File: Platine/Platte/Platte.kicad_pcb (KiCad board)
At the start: 2 copper layers, 31.1 x 31.1 mm, 9 parts, among them J1 Conn_01x07_MountingPin

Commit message: Changes to plate PCB
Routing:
- added copper zone on B.Cu, net /analog_inp_high3
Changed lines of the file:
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@@
 		)
-	)
-	(gr_line
-		(start 85.75 65.75)
-		(end 111 65.75)
-		(stroke
-			(width 0.2)
-			(type default)
-		)
-		(layer "B.Cu")
-		(net 9)
 	)
 	(gr_arc
@@
 			(type default)
 		)
-		(layer "B.Paste")
+		(layer "B.Cu")
+		(net 12)
+	)
+	(gr_line
+		(start 85.75 65.75)
+		(end 111 65.75)
+		(stroke
+			(width 0.2)
+			(type default)
+		)
+		(layer "B.Cu")
+		(net 9)
 	)
 	(gr_arc
 		(start 85.720434 65.708995)
-		(mid 98.354418 56.213174)
+		(mid 98.354418 56.213173)
 		(end 111 65.693544)
 		(stroke
@@
 			(type default)
 		)
-		(layer "B.Paste")
+		(layer "B.Cu")
+		(net 9)
 	)
 	(gr_line
@@
 			(type default)
 		)
-		(layer "B.Paste")
+		(layer "B.Cu")
+		(net 10)
 	)
 	(gr_line
@@
 			(type default)
 		)
-		(layer "B.Paste")
+		(layer "B.Cu")
+		(net 12)
 	)
 	(gr_line
@@
 			(type default)
 		)
-		(layer "B.Paste")
+		(layer "B.Cu")
+		(net 10)
 	)
 	(gr_line
@@
 			(type default)
 		)
-		(layer "B.Paste")
+		(layer "B.Cu")
+		(net 10)
 	)
 	(gr_line
-		(start 85.75 67.5)
-		(end 111 67.5)
+		(start 91.5 67.5)
+		(end 97.25 67.5)
 		(stroke
 			(width 0.2)
 			(type default)
 		)
-		(layer "B.Paste")
+		(layer "B.Cu")
+		(net 10)
 	)
 	(gr_circle
@@
 			(pts
 				(xy 94.75 60.25) (xy 94.75 81.75) (xy 103.75 81.75) (xy 111 74.5) (xy 111 62.75) (xy 108.5 60.25)
-				(xy 94.75 60.25)
 			)
 		)
@@
 		(layer "B.Cu")
 		(hatch edge 0.5)
+		(priority 4)
 		(connect_pads
 			(clearance 0.5)
@@
 		(polygon
 			(pts
-				(xy 111 65.75) (xy 86 65.75) (xy 86 62.75) (xy 93.25 56) (xy 103.5 56) (xy 111 62.75)
+				(xy 85.75 65.75) (xy 111 65.75) (xy 110 63.25) (xy 109 61.5) (xy 107.25 59.75) (xy 105.5 58.25)
+				(xy 103 57) (xy 101.5 56.5) (xy 98.25 56.25) (xy 95.75 56.5) (xy 93.75 57) (xy 92.25 57.75) (xy 90.25 59)
+				(xy 88.5 60.75) (xy 87.5 62) (xy 86.75 63.25) (xy 86.25 64.25)
+			)
+		)
+	)
+	(zone
+		(net 12)
+		(net_name "/analog_inp_high3")
+		(layer "B.Cu")
+		(hatch edge 0.5)
+		(priority 3)
+		(connect_pads
+			(clearance 0.5)
+		)
+		(min_thickness 0.25)
+		(filled_areas_thickness no)
+		(fill yes
+			(thermal_gap 0.5)
+			(thermal_bridge_width 0.5)
+		)
+		(polygon
+			(pts
+				(xy 111 74.25) (xy 86 74.25) (xy 86 74.75) (xy 86.25 75) (xy 86.25 75.25) (xy 86.5 75.5) (xy 86.5 75.75)
+				(xy 86.75 76) (xy 86.75 76.25) (xy 87 76.5) (xy 87 76.75) (xy 87.25 77) (xy 87.4 77) (xy 87.4 77.2)
+				(xy 87.8 77.6) (xy 87.8 77.8) (xy 88 77.8) (xy 88 78.2) (xy 88.2 78.2) (xy 88.6 78.6) (xy 88.6 78.8)
+				(xy 88.8 79) (xy 89 79) (xy 89 79.2) (xy 89.2 79.2) (xy 89.2 79.4) (xy 89.4 79.4) (xy 90 80) (xy 90.4 80.2)
+				(xy 90.8 80.6) (xy 92.4 81.4) (xy 93 81.8) (xy 94.8 82.4) (xy 96.6 82.8) (xy 99.2 83) (xy 101.6 82.6)
+				(xy 103.8 81.8) (xy 105.8 80.8) (xy 107.2 79.8) (xy 108.8 78) (xy 109.6 77) (xy 110.2 76.2) (xy 110.8 74.8)
+				(xy 111 74.2)
 			)
 		)
@@
 		(polygon
 			(pts
-				(xy 111 64.75) (xy 86 64.75) (xy 86 64.25) (xy 86.5 63.75) (xy 86.5 62.75) (xy 87.75 61.5) (xy 87.75 61)
-				(xy 89.75 59) (xy 90.25 59) (xy 93.25 56) (xy 103.5 56) (xy 110.75 63.25) (xy 111 63.25)
+				(xy 111 74.25) (xy 110.25 76) (xy 108.25 78.75) (xy 106.25 80.5) (xy 104.5 81.5) (xy 103.5 82) (xy 100.5 82.75)
+				(xy 99 83) (xy 95 82.5) (xy 92.75 81.75) (xy 89.75 79.75) (xy 87.75 77.75) (xy 87 76.75) (xy 86 74.75)
+				(xy 85.8 74.2)
 			)
 		)
+	)
+	(zone
+		(net 0)
+		(net_name "")
+		(layer "B.Mask")
+		(hatch edge 0.5)
+		(connect_pads
+			(clearance 0.5)
+		)
+		(min_thickness 0.25)
+		(filled_areas_thickness no)
+		(fill yes
+			(thermal_gap 0.5)
+			(thermal_bridge_width 0.5)
+		)
+		(polygon
+			(pts
+				(xy 111 65.75) (xy 85.75 65.75) (xy 86.25 64.25) (xy 86.75 63.25) (xy 88.25 61) (xy 90 59.25) (xy 92.25 57.75)
+				(xy 93.25 57.25) (xy 94.75 56.75) (xy 96 56.5) (xy 98 56.25) (xy 99.75 56.25) (xy 101.75 56.75)
+				(xy 103.5 57.25) (xy 105 58) (xy 107 59.5) (xy 109 61.5) (xy 110.25 63.75) (xy 110.75 65)
+			)
+		)

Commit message: Plate PCB almost done
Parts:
- moved C1 0.96 mm to (88.8, 73.2), turned to -90 degrees
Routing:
- net /analog_inp_high2: track 2.09 -> 8.81 mm, vias 0 -> 5
- net /analog_inp_high3: track 1.79 -> 6.03 mm, vias 0 -> 3
- net GNDA: track 15.3 -> 17.6 mm
- net /analog_inp_high1: track 5.12 -> 7.17 mm, vias 2 -> 4
- net +3.3V: track 45.5 -> 44.5 mm
- added copper zone on B.Cu, net /analog_inp_high2
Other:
- board text added: "I 3.3V O Clk O Da1 O Da2 O Da3 O GNDD I GNDA"
- board text added: "Platte v1.0 EST RUB"

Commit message: small changes
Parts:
- J1: value Conn_01x07_MountingPin -> Conn_01x08_MountingPin; footprint Connector_JST:JST_GH_BM07B-GHS-TBT_1x07-1MP_P1.25mm_Vertical -> Connector_JST:JST_GH_BM08B-GHS-TBT_1x08-1MP_P1.25mm_Vertical
- R1, R2, R3: footprint Resistor_SMD:R_01005_0402Metric_Pad0.57x0.30mm_HandSolder -> Resistor_SMD:R_0201_0603Metric_Pad0.64x0.40mm_HandSolder
- moved J1 0.61 mm to (105.2, 68.0)
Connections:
- J1 pad 1: +3.3V -> VCC
- J1 pad 2: /out_clock -> +3.3V
- J1 pad 3: /amp_data1 -> /out_clock
- J1 pad 4: /amp_data2 -> /amp_data1
- J1 pad 5: /amp_data3 -> /amp_data2
- J1 pad 6: GNDD -> /amp_data3
- J1 pad 7: GNDA -> GNDD
- R1 pad 1: /analog_inp_low1 -> VCC
- R2 pad 1: /analog_inp_low2 -> VCC
- R3 pad 1: /analog_inp_low3 -> VCC
- U1 pad 3: /analog_inp_low1 -> VCC
- U2 pad 3: /analog_inp_low2 -> VCC
- U3 pad 3: /analog_inp_low3 -> VCC
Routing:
- net VCC: track 0.00 -> 6.01 mm
- net /analog_inp_low1: track 2.04 -> 0.00 mm
- net /analog_inp_low2: track 2.01 -> 0.00 mm
- net /analog_inp_low3: track 1.96 -> 0.00 mm
- net /analog_inp_high1: track 7.17 -> 6.17 mm
- net /analog_inp_high3: track 6.03 -> 5.08 mm
- net /analog_inp_high2: track 8.81 -> 8.09 mm
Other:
- board text added: "I VPlate I 3.3V O Clk O Da1 O Da2 O Da3 O GNDD I GNDA"
- board text removed: "I 3.3V O Clk O Da1 O Da2 O Da3 O GNDD I GNDA"

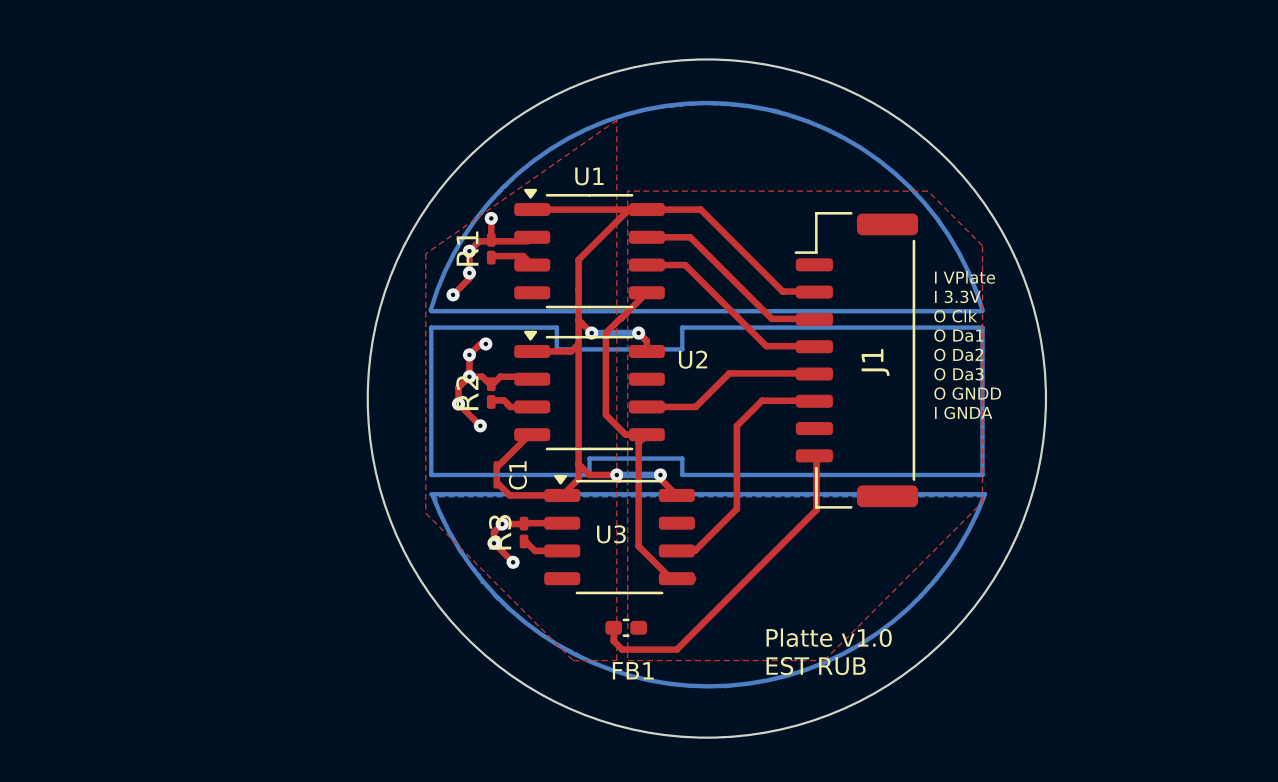
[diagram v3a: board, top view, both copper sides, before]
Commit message: Removing CST simulations because of weight, theyre now in the folder outside the repo
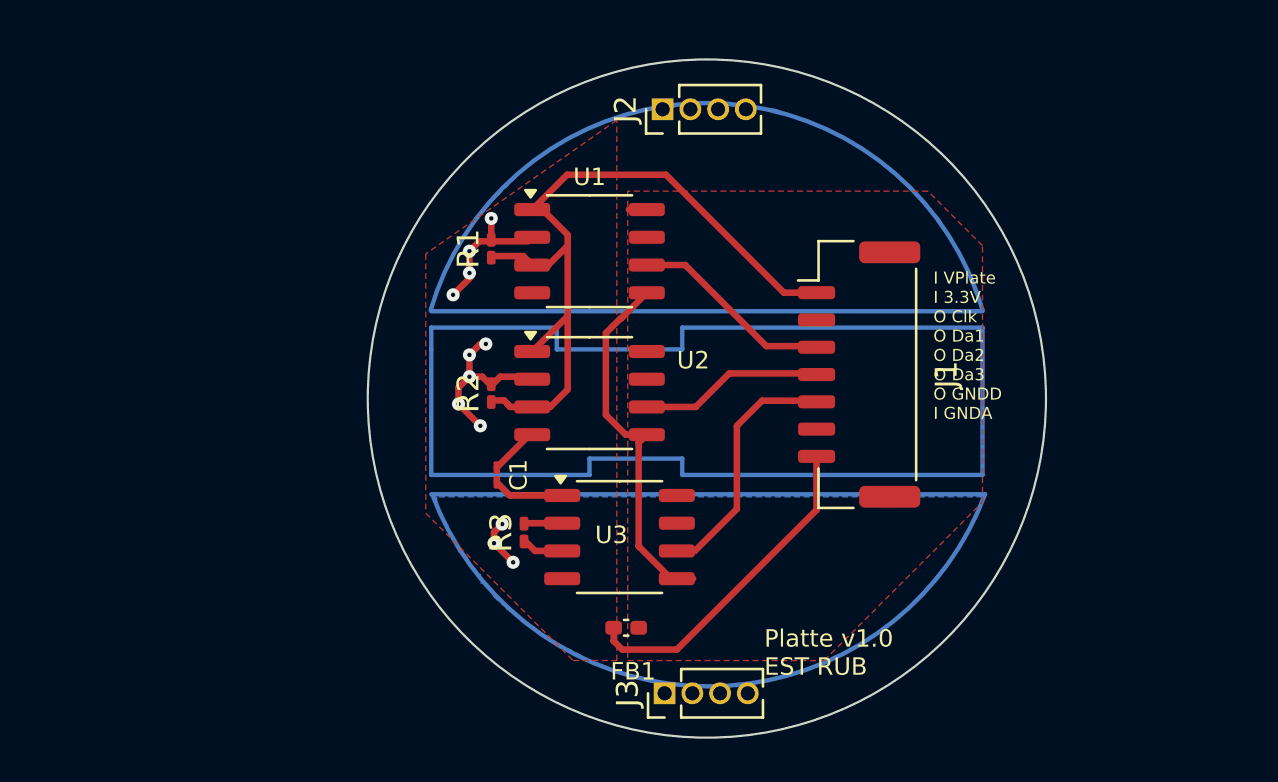
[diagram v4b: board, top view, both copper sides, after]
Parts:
- added J2: Conn_01x04_Socket, Connector_PinHeader_1.27mm:PinHeader_1x04_P1.27mm_Vertical, F.Cu at (96.3, 56.5)
- added J3: Conn_01x04_Socket, Connector_PinHeader_1.27mm:PinHeader_1x04_P1.27mm_Vertical, F.Cu at (96.4, 83.2)
- J1: value Conn_01x08_MountingPin -> Conn_01x07_MountingPin; footprint Connector_JST:JST_GH_BM08B-GHS-TBT_1x08-1MP_P1.25mm_Vertical -> Connector_JST:JST_GH_BM07B-GHS-TBT_1x07-1MP_P1.25mm_Vertical
- moved J1 0.66 mm to (105.3, 68.7)
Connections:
- net /analog_inp_high1 renamed /analog_inp_1
- net /analog_inp_high2 renamed /analog_inp_2
- net /analog_inp_high3 renamed /analog_inp_3
- C1 pad 2: +3.3V -> +3.3VA
- J1 pad 1: VCC -> +3.3VA
- J1 pad 2: +3.3V -> +3.3VD
- J1 pad 3: /out_clock -> /amp_data1
- J1 pad 4: /amp_data1 -> /amp_data2
- J1 pad 5: /amp_data2 -> /amp_data3
- J1 pad 6: /amp_data3 -> GNDD
- J1 pad 7: GNDD -> GNDA
- R1 pad 1: VCC -> +3.3VA
- R2 pad 1: VCC -> +3.3VA
- R3 pad 1: VCC -> +3.3VA
- U1 pad 1: +3.3V -> +3.3VA
- U1 pad 3: VCC -> +3.3VA
- U1 pad 7: /out_clock -> unconnected-(U1-ACLK-Pad7)
- U1 pad 8: +3.3V -> +3.3VD
- U2 pad 1: +3.3V -> +3.3VA
- U2 pad 3: VCC -> +3.3VA
- U2 pad 8: +3.3V -> +3.3VD
- U3 pad 1: +3.3V -> +3.3VA
- U3 pad 3: VCC -> +3.3VA
- U3 pad 8: +3.3V -> +3.3VD
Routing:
- net +3.3V: track 44.5 -> 0.00 mm, vias 4 -> 0
- net +3.3VA: track 0.00 -> 40.6 mm
- net /out_clock: track 9.32 -> 0.00 mm
- net VCC: track 6.01 -> 0.00 mm
- net /analog_inp_3: track 5.08 -> 4.13 mm
- net +3.3VD: track 0.00 -> 0.82 mm

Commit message: PCBs almost finished
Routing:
- net +3.3VD: track 0.82 -> 32.2 mm, vias 0 -> 4
- net +3.3VA: track 40.6 -> 50.1 mm
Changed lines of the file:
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@@
 		)
 		(fp_text user "${REFERENCE}"
-			(at 0 1.905 360)
+			(at 0 1.905 0)
 			(layer "F.Fab")
 			(effects
@@
 		)
 		(fp_text user "${REFERENCE}"
-			(at 0 1.905 360)
+			(at 0 1.905 0)
 			(layer "F.Fab")
 			(effects
@@
 	)
 	(segment
+		(start 91.199999 70.135)
+		(end 91.75 70.685001)
+		(width 0.3)
+		(layer "F.Cu")
+		(net 6)
+	)
+	(segment
 		(start 91.75 74.19)
 		(end 89.3525 74.19)
@@
 	)
 	(segment
+		(start 91.75 74.19)
+		(end 92.89 74.19)
+		(width 0.3)
+		(layer "F.Cu")
+		(net 6)
+	)
+	(segment
+		(start 92.574999 76.73)
+		(end 91.75 76.73)
+		(width 0.3)
+		(layer "F.Cu")
+		(net 6)
+	)
+	(segment
 		(start 89.25 70.02)
 		(end 89.365 70.135)
@@
 	)
 	(segment
+		(start 91.75 70.685001)
+		(end 91.75 74.19)
+		(width 0.3)
+		(layer "F.Cu")
+		(net 6)
+	)
+	(segment
 		(start 91.115 63.635)
 		(end 92 62.75)
@@
 	)
 	(segment
+		(start 90.375 70.135)
+		(end 91.199999 70.135)
+		(width 0.3)
+		(layer "F.Cu")
+		(net 6)
+	)
+	(segment
 		(start 92 62.75)
 		(end 92 62.25)
@@
 	)
 	(segment
-		(start 90.375 70.135)
-		(end 91.199999 70.135)
-		(width 0.3)
-		(layer "F.Cu")
-		(net 6)
-	)
-	(segment
 		(start 89.25 70)
 		(end 89.25 70.02)
@@
 	)
 	(segment
+		(start 93.6 75.704999)
+		(end 92.574999 76.73)
+		(width 0.3)
+		(layer "F.Cu")
+		(net 6)
+	)
+	(segment
 		(start 90.375 61.095)
 		(end 91.97 59.5)
@@
 	)
 	(segment
+		(start 93.6 74.9)
+		(end 93.6 75.704999)
+		(width 0.3)
+		(layer "F.Cu")
+		(net 6)
+	)
+	(segment
 		(start 92 69.334999)
 		(end 92 65.97)
@@
 	)
 	(segment
+		(start 92.89 74.19)
+		(end 93.6 74.9)
+		(width 0.3)
+		(layer "F.Cu")
+		(net 6)
+	)
+	(segment
 		(start 91.75 76.73)
 		(end 90.505 76.73)
@@
 	)
 	(segment
+		(start 93 66.5)
+		(end 92.7 66.2)
+		(width 0.25)
+		(layer "F.Cu")
+		(net 7)
+	)
+	(segment
+		(start 93.8 62.830514)
+		(end 93.8 61.7)
+		(width 0.25)
+		(layer "F.Cu")
+		(net 7)
+	)
+	(segment
+		(start 97 74.19)
+		(end 96.3 73.49)
+		(width 0.25)
+		(layer "F.Cu")
+		(net 7)
+	)
+	(segment
+		(start 96.3 73.49)
+		(end 96.3 73.3)
+		(width 0.25)
+		(layer "F.Cu")
+		(net 7)
+	)
+	(segment
+		(start 92.7 66.2)
+		(end 92.7 63.930514)
+		(width 0.25)
+		(layer "F.Cu")
+		(net 7)
+	)
+	(segment
+		(start 101.75 66.15)
+		(end 103.4 66.15)
+		(width 0.3)
+		(layer "F.Cu")
+		(net 7)
+	)
+	(segment
+		(start 95.625 66.925)
+		(end 95.4 66.7)
+		(width 0.25)
+		(layer "F.Cu")
+		(net 7)
+	)
+	(segment
+		(start 95.625 61.095)
+		(end 96.695 61.095)
+		(width 0.3)
+		(layer "F.Cu")
+		(net 7)
+	)
+	(segment
+		(start 96.695 61.095)
+		(end 101.75 66.15)
+		(width 0.3)
+		(layer "F.Cu")
+		(net 7)
+	)
+	(segment
+		(start 93 72.1)
+		(end 93 66.5)
+		(width 0.25)
+		(layer "F.Cu")
+		(net 7)
+	)
+	(segment
+		(start 94.1 73.2)
+		(end 93 72.1)
+		(width 0.25)
+		(layer "F.Cu")
+		(net 7)
+	)
+	(segment
+		(start 93.8 61.7)
+		(end 94.405 61.095)
+		(width 0.25)
+		(layer "F.Cu")
+		(net 7)
+	)
+	(segment
 		(start 95.625 61.095)
 		(end 94.800001 61.095)
@@
 		(net 7)
 	)
+	(segment
+		(start 94.405 61.095)
+		(end 95.625 61.095)
+		(width 0.25)
+		(layer "F.Cu")
+		(net 7)
+	)
+	(segment
+		(start 95.4 66.7)
+		(end 95.2 66.5)
+		(width 0.25)
+		(layer "F.Cu")
+		(net 7)
+	)
+	(segment
+		(start 95.625 67.595)
+		(end 95.625 66.925)
+		(width 0.25)
+		(layer "F.Cu")
+		(net 7)
+	)
+	(segment
+		(start 92.7 63.930514)
+		(end 93.8 62.830514)
+		(width 0.25)
+		(layer "F.Cu")
+		(net 7)
+	)
+	(via
+		(at 93 66.5)
+		(size 0.6)
+		(drill 0.2)
+		(layers "F.Cu" "B.Cu")
+		(net 7)
+	)
+	(via
+		(at 95.2 66.5)
+		(size 0.6)
+		(drill 0.2)
+		(layers "F.Cu" "B.Cu")
+		(net 7)
+	)
+	(via
+		(at 94.1 73.2)
+		(size 0.6)
+		(drill 0.2)
+		(layers "F.Cu" "B.Cu")
+		(net 7)
+	)
+	(via
+		(at 96.3 73.3)
+		(size 0.6)
+		(drill 0.2)
+		(layers "F.Cu" "B.Cu")
+		(net 7)
+	)
+	(segment
+		(start 94.2 73.3)
+		(end 94.1 73.2)
+		(width 0.25)
+		(layer "B.Cu")
+		(net 7)
+	)
+	(segment
+		(start 96.3 73.3)
+		(end 94.2 73.3)
+		(width 0.25)
+		(layer "B.Cu")
+		(net 7)
+	)
+	(segment
+		(start 95.2 66.5)
+		(end 93 66.5)
+		(width 0.25)
+		(layer "B.Cu")
+		(net 7)
+	)

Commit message: PCBs completely finished
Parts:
- moved J2 1.21 mm to (96.5, 55.3)
- moved J3 0.65 mm to (96.5, 83.9)
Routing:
- net GNDD: track 17.0 -> 18.9 mm, vias 0 -> 1
- net /analog_inp_3: track 4.13 -> 5.13 mm
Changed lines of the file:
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@@
 	)
 	(setup
+		(stackup
+			(layer "F.SilkS"
+				(type "Top Silk Screen")
+			)
+			(layer "F.Paste"
+				(type "Top Solder Paste")
+			)
+			(layer "F.Mask"
+				(type "Top Solder Mask")
+				(thickness 0.01)
+			)
+			(layer "F.Cu"
+				(type "copper")
+				(thickness 0.035)
+			)
+			(layer "dielectric 1"
+				(type "core")
+				(thickness 1.51)
+				(material "FR4")
+				(epsilon_r 4.5)
+				(loss_tangent 0.02)
+			)
+			(layer "B.Cu"
+				(type "copper")
+				(thickness 0.035)
+			)
+			(layer "B.Mask"
+				(type "Bottom Solder Mask")
+				(thickness 0.01)
+			)
+			(layer "B.Paste"
+				(type "Bottom Solder Paste")
+			)
+			(layer "B.SilkS"
+				(type "Bottom Silk Screen")
+			)
+			(copper_finish "None")
+			(dielectric_constraints no)
+		)
 		(pad_to_mask_clearance 0)
 		(allow_soldermask_bridges_in_footprints no)
@@
 		(tags "connector JST GH vertical")
 		(property "Reference" "J1"
-			(at 0 -4 90)
+			(at 0.05 -1.45 90)
 			(layer "F.SilkS")
 			(effects
@@
 	(footprint "Connector_PinHeader_1.27mm:PinHeader_1x04_P1.27mm_Vertical"
 		(layer "F.Cu")
-		(at 96.44 83.25 90)
+		(at 96.49 83.9 90)
 		(descr "Through hole straight pin header, 1x04, 1.27mm pitch, single row")
 		(tags "Through hole pin header THT 1x04 1.27mm single row")
 		(property "Reference" "J3"
-			(at 0 -1.695 90)
+			(at 0 -1.74 90)
 			(layer "F.SilkS")
 			(effects
 				(font
-					(size 1 1)
+					(size 0.7 0.7)
 					(thickness 0.15)
 				)
@@
 	(footprint "Connector_PinHeader_1.27mm:PinHeader_1x04_P1.27mm_Vertical"
 		(layer "F.Cu")
-		(at 96.35 56.5 90)
+		(at 96.46 55.3 90)
 		(descr "Through hole straight pin header, 1x04, 1.27mm pitch, single row")
 		(tags "Through hole pin header THT 1x04 1.27mm single row")
 		(property "Reference" "J2"
-			(at 0 -1.695 90)
+			(at -0.5 -1.96 90)
 			(layer "F.SilkS")
 			(effects
@@
 	)
 	(segment
+		(start 95.625 64.905)
+		(end 96.6 65.88)
+		(width 0.3)
+		(layer "F.Cu")
+		(net 2)
+	)
+	(segment
 		(start 96.733738 78)
 		(end 97 78)
@@
 	)
 	(segment
+		(start 96.6 65.88)
+		(end 96.6 66.4)
+		(width 0.3)
+		(layer "F.Cu")
+		(net 2)
+	)
+	(segment
 		(start 95.25 71.78)
 		(end 95.25 76.516262)
@@
 		(net 2)
 	)
+	(via
+		(at 96.6 66.4)
+		(size 0.6)
+		(drill 0.2)
+		(layers "F.Cu" "B.Cu")
+		(net 2)
+	)
 	(segment
-		(start 97.385 63.635)
+		(start 97.735 63.635)
 		(end 95.625 63.635)
 		(width 0.3)
@@
 	(segment
 		(start 103.4 67.35)
-		(end 101.1 67.35)
+		(end 101.45 67.35)
 		(width 0.3)
 		(layer "F.Cu")
@@
 	)
 	(segment
-		(start 101.1 67.35)
-		(end 97.385 63.635)
+		(start 101.45 67.35)
+		(end 97.735 63.635)
 		(width 0.3)
 		(layer "F.Cu")
@@
 	)
 	(segment
-		(start 99.4 68.6)
-		(end 103.4 68.6)
+		(start 95.625 70.135)
+		(end 99.265 70.135)
 		(width 0.3)
 		(layer "F.Cu")
@@
 	)
 	(segment
-		(start 95.625 70.135)
-		(end 97.865 70.135)
+		(start 100.8 68.6)
+		(end 103.4 68.6)
 		(width 0.3)
 		(layer "F.Cu")
@@
 	)
 	(segment
-		(start 97.865 70.135)
-		(end 99.4 68.6)
+		(start 99.265 70.135)
+		(end 100.8 68.6)
 		(width 0.3)
 		(layer "F.Cu")
@@
 	)
 	(segment
+		(start 90 75.48)
+		(end 89.02 75.48)
+		(width 0.3)
+		(layer "F.Cu")
+		(net 22)
+	)
+	(segment
 		(start 89 75.5)
 		(end 88.625 75.875)
@@
 		(width 0.3)
 		(layer "F.Cu")
+		(net 22)
+	)
+	(segment
+		(start 89.02 75.48)
+		(end 89 75.5)
+		(width 0.3)
+		(layer "F.Cu")
